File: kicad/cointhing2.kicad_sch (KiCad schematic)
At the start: 26 parts, among them J1 USB_B_Micro, Q1 BC847BS, Q2 S8050_J3Y, U1 CP2102-GMR_NRND, U2 ESP-12E, U3 AMS1117-3.3

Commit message: PCB update
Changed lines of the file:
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@@
     (stroke (width 0) (type default) (color 0 0 0 0))
   )
-  (wire (pts (xy 217.17 129.54) (xy 217.17 140.97))
+  (wire (pts (xy 217.17 118.11) (xy 217.17 140.97))
     (stroke (width 0) (type default) (color 0 0 0 0))
   )
@@
     (pin "1")
   )
-  (symbol (lib_id "power:+3V3") (at 217.17 129.54 0) (unit 1)
-    (in_bom yes) (on_board yes)
-    (property "Reference" "#PWR014" (id 0) (at 217.17 133.35 0)
-      (effects (font (size 1.27 1.27)) hide)
-    )
-    (property "Value" "+3V3" (id 1) (at 217.551 125.1458 0))
-    (property "Footprint" "" (id 2) (at 217.17 129.54 0)
-      (effects (font (size 1.27 1.27)) hide)
-    )
-    (property "Datasheet" "" (id 3) (at 217.17 129.54 0)
-      (effects (font (size 1.27 1.27)) hide)
-    )
+  (symbol (lib_id "power:+3V3") (at 217.17 118.11 0) (unit 1)
+    (in_bom yes) (on_board yes)
+    (property "Reference" "#PWR014" (id 0) (at 217.17 121.92 0)
+      (effects (font (size 1.27 1.27)) hide)
+    )
+    (property "Value" "+3V3" (id 1) (at 217.551 113.7158 0))
+    (property "Footprint" "" (id 2) (at 217.17 118.11 0)
+      (effects (font (size 1.27 1.27)) hide)
+    )
+    (property "Datasheet" "" (id 3) (at 217.17 118.11 0)
+      (effects (font (size 1.27 1.27)) hide)
+    )

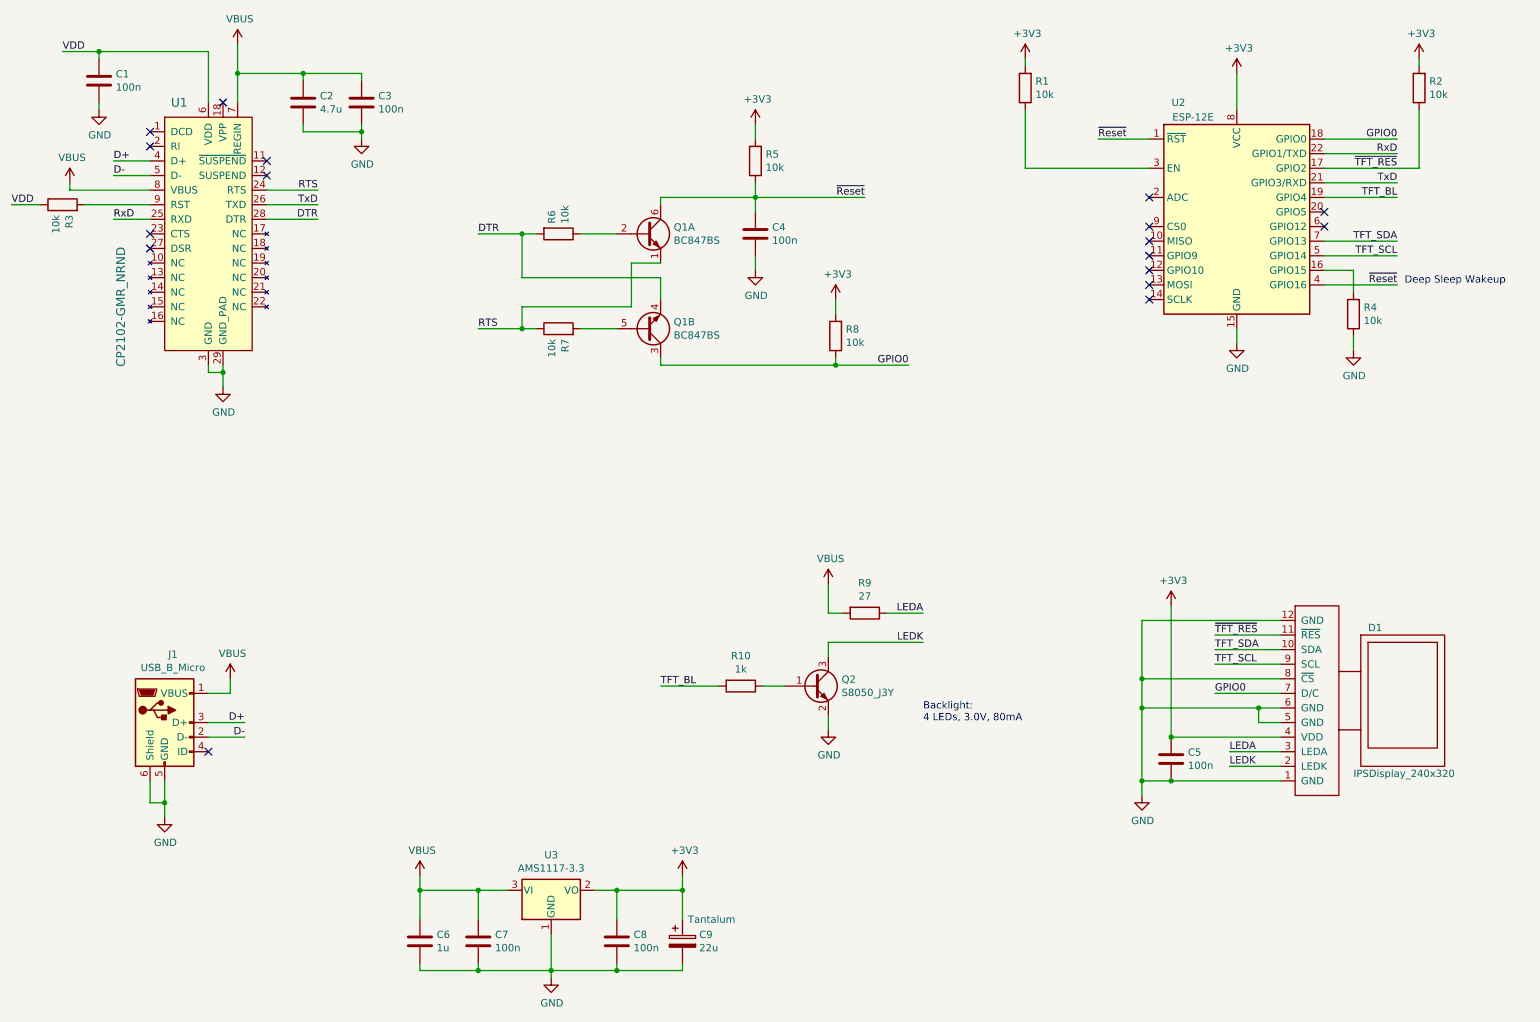
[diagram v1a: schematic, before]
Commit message: Schematic: new diode from GPIO16 to RESET
In order for the deep sleep wake up will work with the auto programming circuit
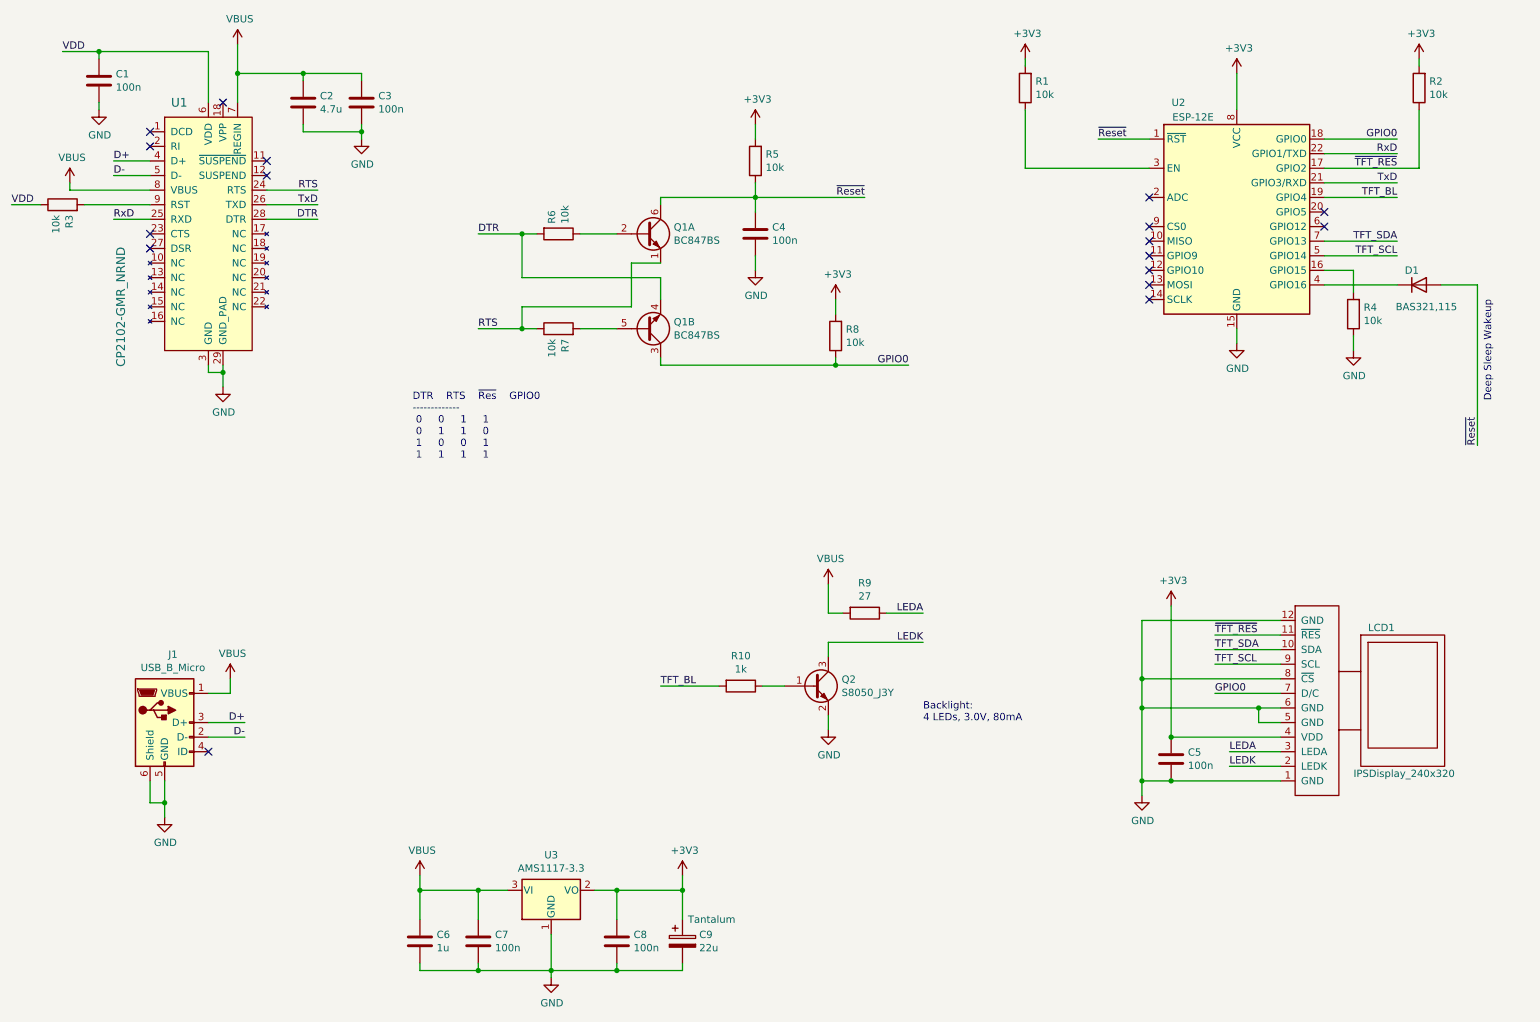
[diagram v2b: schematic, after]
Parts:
- added D1: BAS321,115, Diode_SMD:D_SOD-323, symbol barn53-kicad6:BAS321,115
- LCD1: renamed from D1; now left out of the parts list
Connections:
- net ~{Reset}: now also D1.2 (A); no longer U2.4 (GPIO16)
- new net: D1.1 (K), U2.4 (GPIO16)
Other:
- note added: "DTR RTS ~{Res} GPIO0 ------------- 0 0 1 1 0 1 1 0 1 0 0 1 1 1 1 1"
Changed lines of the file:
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@@
   (title_block
     (title "CoinThing 2\" ESP8266")
-    (date "2021-11-23")
-    (rev "rev.A")
+    (date "2022-10-30")
+    (rev "rev.C")
     (company "barn53")
   )
@@
     (stroke (width 0) (type default) (color 0 0 0 0))
   )
+  (wire (pts (xy 264.16 62.23) (xy 270.51 62.23))
+    (stroke (width 0) (type default) (color 0 0 0 0))
+  )
   (wire (pts (xy 144.78 57.15) (xy 144.78 59.69))
     (stroke (width 0) (type default) (color 0 0 0 0))
@@
     (stroke (width 0) (type default) (color 0 0 0 0))
   )
+  (wire (pts (xy 270.51 62.23) (xy 270.51 90.17))
+    (stroke (width 0) (type default) (color 0 0 0 0))
+  )
   (wire (pts (xy 25.4 44.45) (xy 25.4 45.72))
     (stroke (width 0) (type default) (color 0 0 0 0))
@@
     (stroke (width 0) (type default) (color 0 0 0 0))
   )
-  (text "Deep Sleep Wakeup" (at 257.81 62.23 0)
+  (text "DTR	RTS	~{Res}	GPIO0\n-------------\n 0	 0	 1	 1\n 0	 1	 1	 0\n 1	 0	 0	 1\n 1	 1	 1	 1"
+    (at 85.09 92.71 0)
+    (effects (font (size 1.27 1.27)) (justify left bottom))
+  )
+  (text "Deep Sleep Wakeup" (at 273.05 82.55 90)
     (effects (font (size 1.27 1.27)) (justify left bottom))
   )
@@
     (effects (font (size 1.27 1.27)) (justify right bottom))
   )
-  (label "~{Reset}" (at 256.54 62.23 180)
-    (effects (font (size 1.27 1.27)) (justify right bottom))
+  (label "~{Reset}" (at 270.51 90.17 90)
+    (effects (font (size 1.27 1.27)) (justify left bottom))
   )
   (label "TFT_BL" (at 128.27 132.08 0)
@@
   )
   (symbol (lib_id "barn53-kicad:IPSDisplay_240x320") (at 236.22 148.59 0) (unit 1)
-    (in_bom yes) (on_board yes)
-    (property "Reference" "D1" (id 0) (at 251.46 121.92 0)
+    (in_bom no) (on_board yes)
+    (property "Reference" "LCD1" (id 0) (at 251.46 121.92 0)
       (effects (font (size 1.27 1.27)) (justify left))
     )
@@
     (pin "2")
     (pin "6")
-  )
-  (symbol (lib_id "Transistor_BJT:BC847BS") (at 125.73 69.85 0) (mirror x) (unit 2)
-    (in_bom yes) (on_board yes)
-    (property "Reference" "Q1" (id 0) (at 130.556 68.6816 0)
-      (effects (font (size 1.27 1.27)) (justify left))
-    )
-    (property "Value" "BC847BS" (id 1) (at 130.556 70.993 0)
-      (effects (font (size 1.27 1.27)) (justify left))
-    )
-    (property "Footprint" "Package_TO_SOT_SMD:SOT-363_SC-70-6" (id 2) (at 130.81 72.39 0)
-      (effects (font (size 1.27 1.27)) hide)
-    )
-    (property "Datasheet" "https://assets.nexperia.com/documents/data-sheet/BC847BS.pdf" (id 3) (at 125.73 69.85 0)
-      (effects (font (size 1.27 1.27)) hide)
-    )
-    (property "LCSC" "C8653" (id 4) (at 125.73 69.85 0)
-      (effects (font (size 1.27 1.27)) hide)
-    )
     (pin "3")
     (pin "4")
     (pin "5")
   )
+  (symbol (lib_id "Transistor_BJT:BC847BS") (at 125.73 69.85 0) (mirror x) (unit 2)
+    (in_bom yes) (on_board yes)
+    (property "Reference" "Q1" (id 0) (at 130.556 68.6816 0)
+      (effects (font (size 1.27 1.27)) (justify left))
+    )
+    (property "Value" "BC847BS" (id 1) (at 130.556 70.993 0)
+      (effects (font (size 1.27 1.27)) (justify left))
+    )
+    (property "Footprint" "Package_TO_SOT_SMD:SOT-363_SC-70-6" (id 2) (at 130.81 72.39 0)
+      (effects (font (size 1.27 1.27)) hide)
+    )
+    (property "Datasheet" "https://assets.nexperia.com/documents/data-sheet/BC847BS.pdf" (id 3) (at 125.73 69.85 0)
+      (effects (font (size 1.27 1.27)) hide)
+    )
+    (property "LCSC" "C8653" (id 4) (at 125.73 69.85 0)
+      (effects (font (size 1.27 1.27)) hide)
+    )
+    (pin "1")
+    (pin "2")
+    (pin "6")
+    (pin "3")
+    (pin "4")
+    (pin "5")
+  )
   (symbol (lib_id "Device:C") (at 96.52 176.53 0) (unit 1)
     (in_bom yes) (on_board yes)
@@
     )
     (pin "1")
+  )
+  (symbol (lib_id "barn53-kicad6:BAS321,115") (at 260.35 62.23 0) (unit 1)
+    (in_bom yes) (on_board yes)
+    (property "Reference" "D1" (id 0) (at 259.08 59.69 0))
+    (property "Value" "BAS321,115" (id 1) (at 261.62 66.04 0))
+    (property "Footprint" "Diode_SMD:D_SOD-323" (id 2) (at 260.35 66.675 0)
+      (effects (font (size 1.27 1.27)) hide)
+    )
+    (property "Datasheet" "https://datasheet.lcsc.com/lcsc/1811081810_Nexperia-BAS321-115_C24372.pdf" (id 3) (at 260.35 72.39 0)
+      (effects (font (size 1.27 1.27)) hide)
+    )
+    (property "LCSC" "C24372" (id 4) (at 260.35 59.7972 0)
+      (effects (font (size 1.27 1.27)) hide)
+    )
+    (pin "1")
+    (pin "2")
   )
   (sheet_instances
@@
       (reference "C9") (unit 1) (value "22u") (footprint "Capacitor_Tantalum_SMD:CP_EIA-3216-18_Kemet-A")
     )
-    (path "/00000000-0000-0000-0000-0000619d7b2a"
-      (reference "D1") (unit 1) (value "IPSDisplay_240x320") (footprint "barn53-kicad:IPS_Display_240x320_FPC_105deg")
+    (path "/d3b12071-a811-41a7-8738-a6d39531c182"
+      (reference "D1") (unit 1) (value "BAS321,115") (footprint "Diode_SMD:D_SOD-323")
     )
     (path "/00000000-0000-0000-0000-00005db8ff43"
       (reference "J1") (unit 1) (value "USB_B_Micro") (footprint "barn53-kicad:MicroUSB_through_hole_fixing")
     )
+    (path "/00000000-0000-0000-0000-0000619d7b2a"
+      (reference "LCD1") (unit 1) (value "IPSDisplay_240x320") (footprint "barn53-kicad:IPS_Display_240x320_FPC_105deg")
+    )
     (path "/00000000-0000-0000-0000-000061a6c31c"
